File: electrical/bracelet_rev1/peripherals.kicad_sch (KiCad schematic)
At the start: 4 parts, among them U2 LSM6DSO32TR

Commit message: Many schematic updates
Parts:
- removed R2: 0, symbol Device:R
- removed U2: LSM6DSO32TR, LGA-14L_2P5X3X0P83_STM, symbol IMU:LSM6DSO32TR
- added BZ1: Buzzer, symbol Device:Buzzer
- added C20: 10uF, symbol Device:C
- added C21, C23, C28: 0.1uF, symbol Device:C
- added C22: 4.7uF, symbol Device:C
- added D4: WS2812B, LED_SMD:LED_WS2812B_PLCC4_5.0x5.0mm_P3.2mm, symbol LED:WS2812B
- added R14, R15: 0, symbol Device:R
- added SW2: SW_MEC_5E, symbol Switch:SW_MEC_5E
- added U2: TXS0101DBV, Package_TO_SOT_SMD:SOT-23-6, symbol Logic_LevelTranslator:TXS0101DBV
- added U5: LSM6DS3, Package_LGA:LGA-14_3x2.5mm_P0.5mm_LayoutBorder3x4y, symbol Sensor_Motion:LSM6DS3
- added U7: MAX30102, OptoDevice:Maxim_OLGA-14_3.3x5.6mm_P0.8mm, symbol Sensor:MAX30102
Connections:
- net GND: now also BZ1.2 (-), C20.2, C21.2, C22.2, C23.2, C28.2, D4.3 (VSS), SW2.1, SW2.2, U2.2 (GND), U5.1 (SDO/SA0), U5.2 (SDX), U5.3 (SCX), U5.6 (GND), U5.7 (GND), U7.12 (GND), U7.4 (PGND)
- net IMU_INT1: now also U5.4 (INT1)
- net IMU_INT2: now also U5.9 (INT2)
- net SCL: now also U5.13 (SCL), U7.2 (SCL)
- net SDA: now also U5.14 (SDA), U7.3 (SDA)
- net VDD renamed 1V8
- net 1V8: now also C22.1, C23.1, R14.1, R15.1, U2.1 (V_{CCA}), U2.5 (OE), U5.5 (VDDIO), U5.8 (VDD), U7.11 (VDD)
- new net: D4.4 (DIN), U2.4 (B)
- new net: R14.2, U5.12 (CS)
- new net 3V3: C20.1, C21.1, D4.1 (VDD), U2.6 (V_{CCB}), U7.10 (VLED+), U7.9 (VLED+)
- new net BUZZER: BZ1.1 (+)
- new net POX_INT: U7.13 (~{INT})
- new net USER_BUTTON: C28.1, R15.2, SW2.3 (K), SW2.4 (A)
- new net WS2812_DIN: U2.3 (A)
- no-connect marks 0 -> 1
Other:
- moved on the sheet: C14, C15

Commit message: Mostly finihsed hopefully but still needs clean up anyway
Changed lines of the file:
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@@
-		)
-	)
-	(label "IMU_INT2"
-		(at 90.17 81.28 0)
-		(effects
-			(font
-				(size 1.27 1.27)
-			)
-			(justify left bottom)
-		)
-	)
-	(label "IMU_INT1"
-		(at 90.17 78.74 0)
-		(effects
-			(font
-				(size 1.27 1.27)
-			)
-			(justify left bottom)
 		)
 	)
@@
 		)
 	)
+	(global_label "IMU_INT2"
+		(shape output)
+		(at 99.06 81.28 0)
+		(fields_autoplaced yes)
+		(effects
+			(font
+				(size 1.27 1.27)
+			)
+			(justify left)
+		)
+		(property "Intersheetrefs" "${INTERSHEET_REFS}"
+			(at 110.5119 81.28 0)
+			(effects
+				(font
+					(size 1.27 1.27)
+				)
+				(justify left)
+				(hide yes)
+			)
+		)
+	)
 	(global_label "BUZZER"
 		(shape input)
@@
 				(hide yes)
 			)
+		)
+	)
+	(global_label "IMU_INT1"
+		(shape output)
+		(at 99.06 78.74 0)
+		(fields_autoplaced yes)
+		(effects
+			(font
+				(size 1.27 1.27)
+			)
+			(justify left)
+		)
+		(property "Intersheetrefs" "${INTERSHEET_REFS}"
+			(at 110.5119 78.74 0)
+			(effects
+				(font
+					(size 1.27 1.27)
+				)
+				(justify left)
+				(hide yes)
+			)

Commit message: May updates
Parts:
- added C30, C31: 100nF, symbol Device:C
- added U10: BMP390L, 10LGA_2X2X0p75_BOS, symbol Barometer:BMP390L
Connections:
- net 1V8: now also C30.1, C31.1, U10.1 (VDDIO), U10.10 (VDD), U10.6 (CSB)
- net GND: now also C30.2, C31.2, U10.3 (VSS), U10.5 (SDO), U10.8 (VSS), U10.9 (VSS)
- net SCL: now also U10.2 (SCK)
- net SDA: now also U10.4 (SDI)
- new net BMP_IT: U10.7 (INT)
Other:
- note added: "Barometer"
- note added: "Button & Buzzer"
- note added: "Heart Rate / Pulse Ox"
- note added: "IMU"
- note added: "LED"
- moved on the sheet: BZ1, C14, C15, C20, C21, C22, C23, C28, D4, R14, R15, SW2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

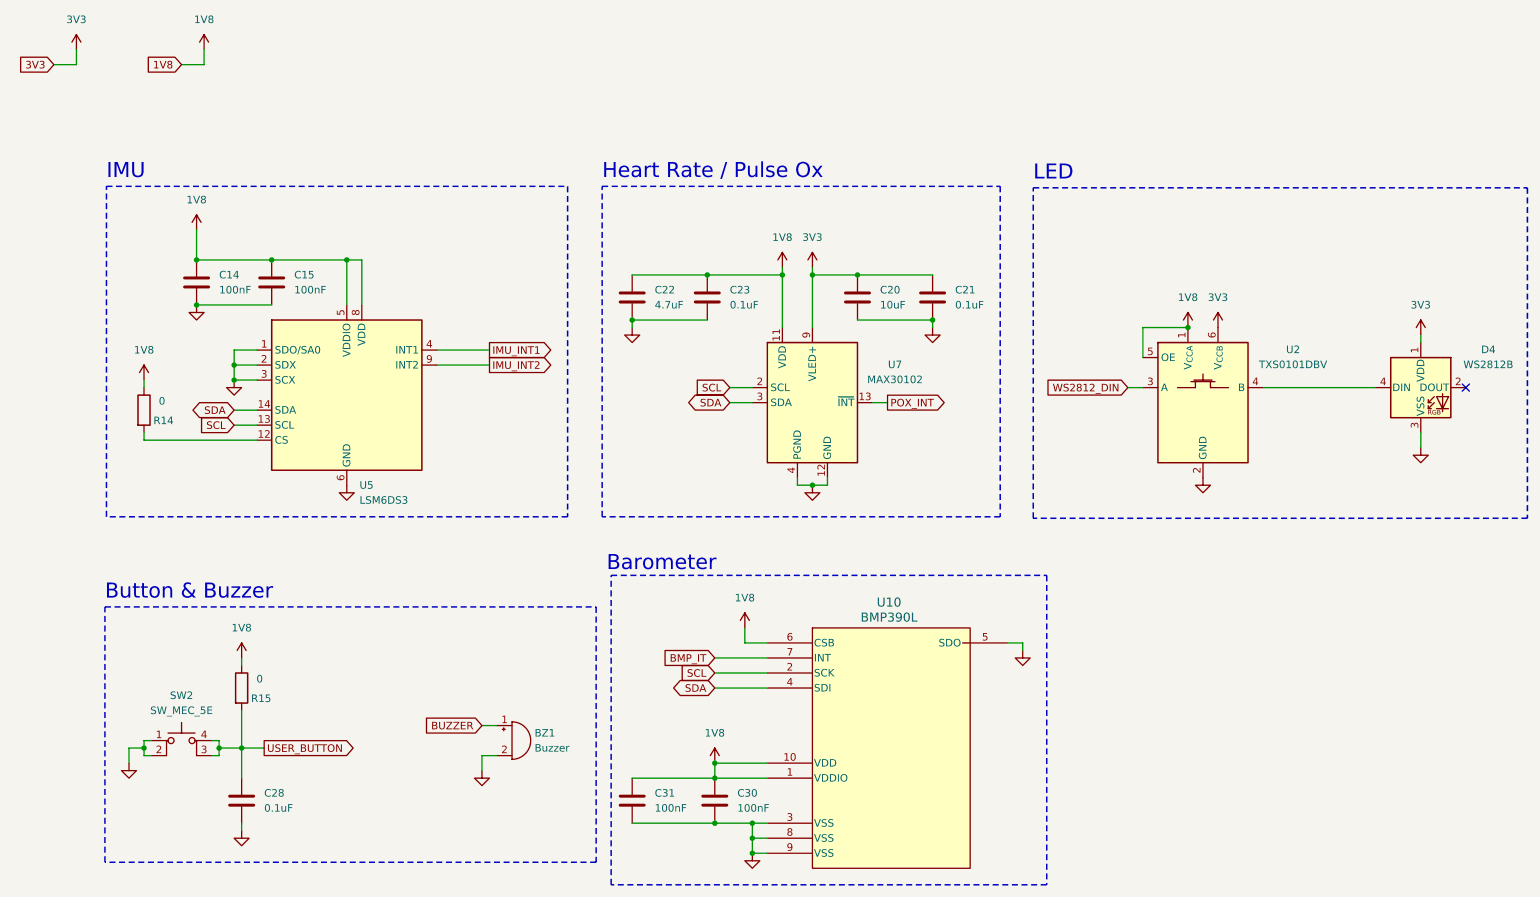
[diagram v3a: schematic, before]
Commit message: Redo component numbers
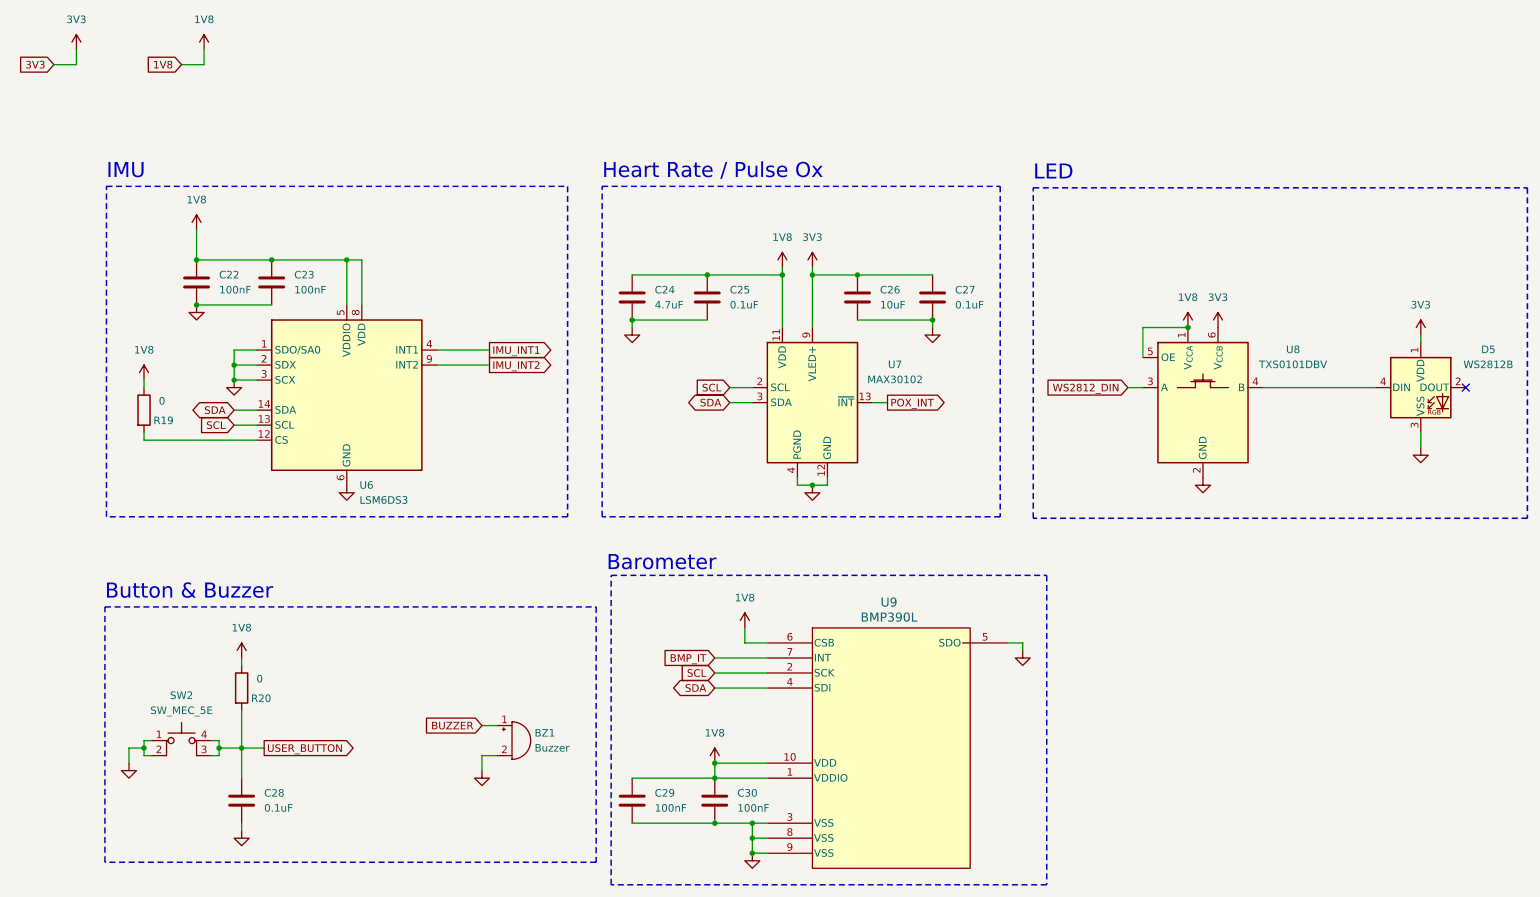
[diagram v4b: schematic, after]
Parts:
- renumbered C14 to C22, C15 to C23, C22 to C24, C23 to C25, C20 to C26, C21 to C27, C31 to C29, D4 to D5, R14 to R19, R15 to R20, U5 to U6, U2 to U8, U10 to U9

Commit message: Updated more things
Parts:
- removed D5: WS2812B, LED_SMD:LED_WS2812B_PLCC4_5.0x5.0mm_P3.2mm, symbol LED:WS2812B
- removed U8: TXS0101DBV, Package_TO_SOT_SMD:SOT-23-6, symbol Logic_LevelTranslator:TXS0101DBV
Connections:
- no-connect marks 1 -> 0
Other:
- note removed: "LED"

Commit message: More schematic stuff
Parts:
- added R24: 0, Resistor_SMD:R_0201_0603Metric_Pad0.64x0.40mm_HandSolder, symbol Device:R
- C22, C23, C24, C25, C26, C27, C28, C29, C30: footprint (none) -> Capacitor_SMD:C_0603_1608Metric_Pad1.08x0.95mm_HandSolder
- R19, R20: footprint (none) -> Resistor_SMD:R_0603_1608Metric_Pad0.98x0.95mm_HandSolder
- SW2: footprint (none) -> Button_Switch_SMD:SW_MEC_5GSH9
- U9: footprint 10LGA_2X2X0p75_BOS -> (none)
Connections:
- net GND: now also R24.2; no longer U9.5 (SDO)
- new net: R24.1, U9.5 (SDO)
